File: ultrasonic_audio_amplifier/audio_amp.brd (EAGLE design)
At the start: 65 x 30 mm, 23 parts, among them CON1 MOLEX_5566-2, J1 282834-2, J2 282834-2, J3 MKDS_5/2-6,352, U1 DS1881Z-050+, U2 LM384_AUDIO_POWER_AMP

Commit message: Updated board layout for review
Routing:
- net SCL: track 24.1 -> 22.5 mm
- net SDA: track 21.0 -> 19.9 mm

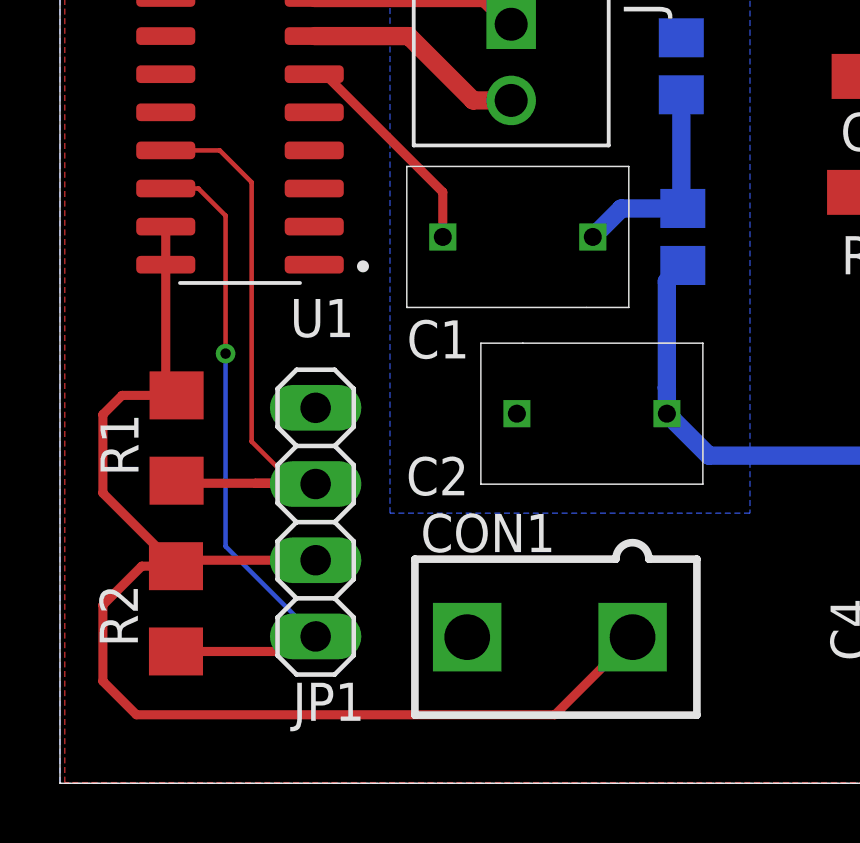
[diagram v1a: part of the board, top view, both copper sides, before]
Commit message: Modified I2C connector
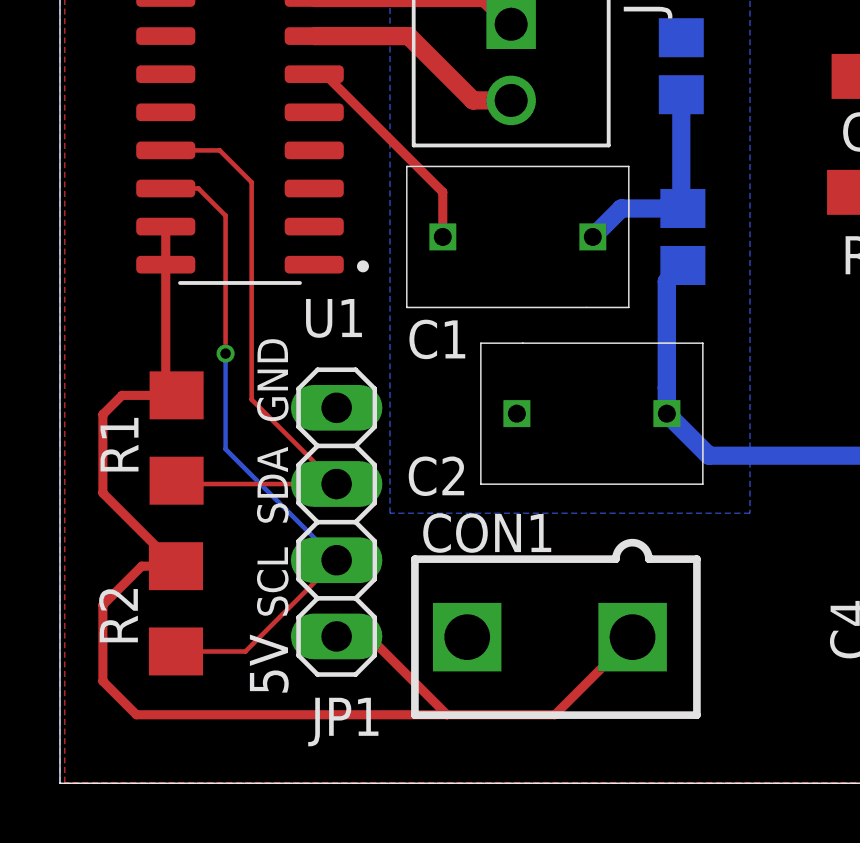
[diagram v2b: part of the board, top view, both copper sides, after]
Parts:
- moved JP1 0.70 mm to (19.2, 30.7)
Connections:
- net 5V: now also JP1.4; no longer JP1.3
- net SCL: now also JP1.3; no longer JP1.4
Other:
- board text added: "5V"
- board text added: "GND"
- board text added: "SCL"
- board text added: "SDA"
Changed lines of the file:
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@@
 <setting verticaltext="up"/>
 </settings>
-<grid distance="0.1" unitdist="mm" unit="mm" style="dots" multiple="1" display="yes" altdistance="0.05" altunitdist="mm" altunit="mm"/>
+<grid distance="3.93700787" unitdist="mil" unit="mil" style="dots" multiple="1" display="yes" altdistance="0.05" altunitdist="mm" altunit="mm"/>
 <layers>
 <layer number="1" name="Top" color="4" fill="1" visible="yes" active="yes"/>
@@
 <wire x1="57.5" y1="23.1" x2="32.5" y2="23.1" width="0.1524" layer="48"/>
 <text x="33" y="23.5" size="1.6764" layer="48">Heatsink Keepout</text>
+<text x="17.6" y="34" size="1.016" layer="25" rot="R90">GND</text>
+<text x="17.6" y="30.6" size="1.016" layer="25" rot="R90">SDA</text>
+<text x="17.6" y="27.5" size="1.016" layer="25" rot="R90">SCL</text>
+<text x="17.6" y="24.9" size="1.27" layer="25" rot="R90">5V</text>
 </plain>
 <attributes>
@@
 </class>
 </classes>
-<designrules name="JLCPCB2Layer">
+<designrules name="OSHPark2Layer">
 <description language="de">&lt;b&gt;EAGLE Design Rules&lt;/b&gt;
 &lt;p&gt;
@@
 <param name="rvMicroViaOuter" value="0.25"/>
 <param name="rvMicroViaInner" value="0.25"/>
-<param name="rlMinPadTop" value="6mil"/>
+<param name="rlMinPadTop" value="5mil"/>
 <param name="rlMaxPadTop" value="20mil"/>
-<param name="rlMinPadInner" value="6mil"/>
+<param name="rlMinPadInner" value="5mil"/>
 <param name="rlMaxPadInner" value="20mil"/>
-<param name="rlMinPadBottom" value="6mil"/>
+<param name="rlMinPadBottom" value="5mil"/>
 <param name="rlMaxPadBottom" value="20mil"/>
-<param name="rlMinViaOuter" value="6mil"/>
+<param name="rlMinViaOuter" value="5mil"/>
 <param name="rlMaxViaOuter" value="20mil"/>
-<param name="rlMinViaInner" value="6mil"/>
+<param name="rlMinViaInner" value="5mil"/>
 <param name="rlMaxViaInner" value="20mil"/>
 <param name="rlMinMicroViaOuter" value="4mil"/>
@@
 <attribute name="NAME" x="59.215" y="36.135" size="1.27" layer="25"/>
 </element>
-<element name="JP1" library="pinhead" library_urn="urn:adsk.eagle:library:325" package="1X04" package3d_urn="urn:adsk.eagle:package:22407/2" value="" x="18.5216" y="30.7038" smashed="yes" rot="R270">
-<attribute name="NAME" x="20.16" y="25.3496" size="1.27" layer="25" ratio="10" rot="R180"/>
-<attribute name="VALUE" x="15.3466" y="35.7838" size="1.27" layer="27" rot="R270"/>
+<element name="JP1" library="pinhead" library_urn="urn:adsk.eagle:library:325" package="1X04" package3d_urn="urn:adsk.eagle:package:22407/2" value="" x="19.2216" y="30.7038" smashed="yes" rot="R270">
+<attribute name="NAME" x="20.76" y="24.8496" size="1.27" layer="25" ratio="10" rot="R180"/>
+<attribute name="VALUE" x="16.0466" y="35.7838" size="1.27" layer="27" rot="R270"/>
 </element>
 <element name="R1" library="resistor" library_urn="urn:adsk.eagle:library:348" package="R1206" package3d_urn="urn:adsk.eagle:package:23540/2" value="1k" x="13.887" y="33.507" smashed="yes" rot="R90">
@@
 <attribute name="MF" value="Maxim Integrated" x="16" y="43.73" size="1.778" layer="27" rot="R180" display="off"/>
 <attribute name="MP" value="DS1881Z-050+" x="16" y="43.73" size="1.778" layer="27" rot="R180" display="off"/>
-<attribute name="NAME" x="19.81" y="38.142" size="1.27" layer="25" rot="R180"/>
+<attribute name="NAME" x="20.21" y="38.142" size="1.27" layer="25" rot="R180"/>
 <attribute name="PACKAGE" value="SOIC-16 Maxim" x="16" y="43.73" size="1.778" layer="27" rot="R180" display="off"/>
 </element>
@@
 <contactref element="U1" pad="15"/>
 <contactref element="U1" pad="16"/>
-<contactref element="JP1" pad="3"/>
 <contactref element="R1" pad="2"/>
 <contactref element="R2" pad="2"/>
-<wire x1="13.929" y1="29.271" x2="14.1038" y2="29.4458" width="0.1524" layer="1"/>
 <contactref element="CON1" pad="1"/>
-<wire x1="29.0859" y1="26.87" x2="26.4983" y2="24.2824" width="0.3048" layer="1"/>
 <wire x1="12.5476" y1="24.2824" x2="11.43" y2="25.4" width="0.3048" layer="1"/>
 <wire x1="11.43" y1="25.4" x2="11.43" y2="27.94" width="0.3048" layer="1"/>
 <wire x1="11.43" y1="27.94" x2="12.7258" y2="29.2358" width="0.3048" layer="1"/>
 <wire x1="12.7258" y1="29.2358" x2="13.866" y2="29.2358" width="0.3048" layer="1"/>
-<wire x1="26.4983" y1="24.2824" x2="12.5476" y2="24.2824" width="0.3048" layer="1"/>
-<wire x1="18.5216" y1="29.4338" x2="14.1158" y2="29.4338" width="0.3048" layer="1"/>
+<wire x1="26.4983" y1="24.2824" x2="22.9" y2="24.2824" width="0.3048" layer="1"/>
+<wire x1="22.9" y1="24.2824" x2="12.5476" y2="24.2824" width="0.3048" layer="1"/>
 <wire x1="13.525" y1="39.285" x2="13.525" y2="40.555" width="0.3048" layer="1"/>
 <wire x1="13.525" y1="39.285" x2="13.525" y2="35.291" width="0.3048" layer="1"/>
@@
 <wire x1="11.43" y1="34.29" x2="11.43" y2="31.6718" width="0.3048" layer="1"/>
 <wire x1="11.43" y1="31.6718" x2="13.866" y2="29.2358" width="0.3048" layer="1"/>
-<wire x1="14.1158" y1="29.4338" x2="14.1038" y2="29.4458" width="0.3048" layer="1"/>
-<wire x1="13.866" y1="29.2358" x2="13.8938" y2="29.2358" width="0.3048" layer="1"/>
-<wire x1="13.8938" y1="29.2358" x2="13.929" y2="29.271" width="0.3048" layer="1"/>
+<contactref element="JP1" pad="4"/>
+<wire x1="29.0859" y1="26.87" x2="26.4983" y2="24.2824" width="0.3048" layer="1"/>
+<wire x1="22.9" y1="24.2824" x2="20.2886" y2="26.8938" width="0.3048" layer="1"/>
+<wire x1="20.2886" y1="26.8938" x2="19.2216" y2="26.8938" width="0.3048" layer="1"/>
 </signal>
 <signal name="SIGNAL_IN">
@@
 </signal>
 <signal name="SCL">
-<contactref element="JP1" pad="4"/>
 <contactref element="R2" pad="1"/>
 <contactref element="U1" pad="14"/>
-<wire x1="13.866" y1="26.3918" x2="18.0196" y2="26.3918" width="0.3048" layer="1"/>
-<wire x1="18.0196" y1="26.3918" x2="18.5216" y2="26.8938" width="0.3048" layer="1"/>
 <wire x1="13.525" y1="41.825" x2="14.6138" y2="41.825" width="0.1524" layer="1"/>
 <wire x1="14.6138" y1="41.825" x2="15.5194" y2="40.9194" width="0.1524" layer="1"/>
+<contactref element="JP1" pad="3"/>
+<wire x1="13.866" y1="26.3918" x2="16.1796" y2="26.3918" width="0.1524" layer="1"/>
+<wire x1="16.1796" y1="26.3918" x2="19.2216" y2="29.4338" width="0.1524" layer="1"/>
+<via x="15.5194" y="36.322" extent="1-16" drill="0.35"/>
+<wire x1="15.5194" y1="36.322" x2="15.5194" y2="33.136" width="0.1524" layer="16"/>
+<wire x1="15.5194" y1="33.136" x2="19.2216" y2="29.4338" width="0.1524" layer="16"/>
 <wire x1="15.5194" y1="40.9194" x2="15.5194" y2="36.322" width="0.1524" layer="1"/>
-<via x="15.5194" y="36.322" extent="1-16" drill="0.35"/>
-<wire x1="15.5194" y1="36.322" x2="15.5194" y2="29.896" width="0.1524" layer="16"/>
-<wire x1="15.5194" y1="29.896" x2="18.5216" y2="26.8938" width="0.1524" layer="16"/>
 </signal>
 <signal name="SDA">
@@
 <contactref element="R1" pad="1"/>
 <contactref element="U1" pad="13"/>
-<wire x1="13.887" y1="32.085" x2="13.9728" y2="31.9992" width="0.3048" layer="1"/>
-<wire x1="13.9728" y1="31.9992" x2="16.51" y2="31.9992" width="0.3048" layer="1"/>
-<wire x1="16.51" y1="31.9992" x2="17.78" y2="31.9992" width="0.3048" layer="1"/>
 <wire x1="16.388" y1="42.032" x2="15.325" y2="43.095" width="0.1524" layer="1"/>
-<wire x1="16.388" y1="42.032" x2="16.388" y2="33.3912" width="0.1524" layer="1"/>
-<wire x1="17.3736" y1="32.4056" x2="17.78" y2="31.9992" width="0.1524" layer="1"/>
-<wire x1="16.388" y1="33.3912" x2="17.3736" y2="32.4056" width="0.1524" layer="1"/>
-<wire x1="16.51" y1="31.9992" x2="18.4962" y2="31.9992" width="0.3048" layer="1"/>
-<wire x1="18.4962" y1="31.9992" x2="18.5216" y2="31.9738" width="0.3048" layer="1"/>
+<wire x1="16.388" y1="42.032" x2="16.388" y2="34.7912" width="0.1524" layer="1"/>
 <wire x1="15.325" y1="43.095" x2="13.525" y2="43.095" width="0.1524" layer="1"/>
+<wire x1="16.388" y1="34.7912" x2="19.2054" y2="31.9738" width="0.1524" layer="1"/>
+<wire x1="19.2054" y1="31.9738" x2="19.2216" y2="31.9738" width="0.1524" layer="1"/>
+<wire x1="13.9982" y1="31.9738" x2="19.2216" y2="31.9738" width="0.1524" layer="1"/>
+<wire x1="13.887" y1="32.085" x2="13.9982" y2="31.9738" width="0.1524" layer="1"/>
 </signal>
 <signal name="SIGNAL_OUT">
